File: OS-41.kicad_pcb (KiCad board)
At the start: 4 copper layers, 26.1 x 58.1 mm, 72 parts, among them J2 Conn_01x02_Pin, J3 Conn_01x02_Pin, J4 Conn_Coaxial, J6 Conn_01x04_Pin, J8 Conn_01x02_Pin, J9 Conn_01x02_Pin, U2 SI4432-B1-FMR, U3 MCP1640x-xCHY, U4 ATGM336H-5N31, U6 BMP390L, U7 STM32F411CEUx, Y1 Crystal_GND24, Y2 Crystal, Y3 Crystal_GND24

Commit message: Final PCB
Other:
- board text added: "BOOT"
- board text added: "RST"
- board text added: "Vin"
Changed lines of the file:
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@@
 		)
 		(property "Footprint" "centdir:ANT_1575AT_JOT"
-			(at 0 0 360)
+			(at 0 0 0)
 			(layer "F.Fab")
 			(hide yes)
@@
 		)
 		(property "Datasheet" ""
-			(at 0 0 360)
+			(at 0 0 0)
 			(layer "F.Fab")
 			(hide yes)
@@
 		)
 		(property "Description" "Antenna"
-			(at 0 0 360)
+			(at 0 0 0)
 			(layer "F.Fab")
 			(hide yes)
@@
 		(tags "capacitor handsolder")
 		(property "Reference" "C29"
-			(at 0.056569 1.06066 360)
+			(at 0.056569 1.06066 0)
 			(layer "F.SilkS")
 			(effects
@@
 		)
 		(property "Value" "1.5pF"
-			(at 0 1.16 360)
+			(at 0 1.16 0)
 			(layer "F.Fab")
 			(effects
@@
 		)
 		(fp_text user "${REFERENCE}"
-			(at 0 0 360)
+			(at 0 0 0)
 			(layer "F.Fab")
 			(effects
@@
 		(layer "Edge.Cuts")
 	)
+	(gr_text "GND"
+		(at 149.9 130.1 0)
+		(layer "B.SilkS")
+		(effects
+			(font
+				(size 1 1)
+				(thickness 0.25)
+				(bold yes)
+			)
+			(justify left bottom mirror)
+		)
+	)
+	(gr_text "Vin"
+		(at 146.3 130.1 0)
+		(layer "B.SilkS")
+		(effects
+			(font
+				(size 1 1)
+				(thickness 0.25)
+				(bold yes)
+			)
+			(justify left bottom mirror)
+		)
+	)
+	(gr_text "RST"
+		(at 128.62 109.9 -90)
+		(layer "B.SilkS")
+		(effects
+			(font
+				(size 1.5 1.5)
+				(thickness 0.3)
+				(bold yes)
+			)
+			(justify left bottom mirror)
+		)
+	)
+	(gr_text "GND"
+		(at 145.2 116.6 -90)
+		(layer "B.SilkS")
+		(effects
+			(font
+				(size 1 1)
+				(thickness 0.25)
+				(bold yes)
+			)
+			(justify left bottom mirror)
+		)
+	)
+	(gr_text "VCC"
+		(at 145.2 113.3 -90)
+		(layer "B.SilkS")
+		(effects
+			(font
+				(size 1 1)
+				(thickness 0.25)
+				(bold yes)
+			)
+			(justify left bottom mirror)
+		)
+	)
 	(gr_text "DIO"
 		(at 148.4 106.6 270)
@@
 		)
 	)
+	(gr_text "BOOT"
+		(at 128.79 100.52 270)
+		(layer "B.SilkS")
+		(effects
+			(font
+				(size 1.5 1.5)
+				(thickness 0.3)
+				(bold yes)
+			)
+			(justify left bottom mirror)
+		)
+	)
 	(gr_text "VCC"
 		(at 148.4 109.9 270)
@@
 			)
 		)
+	)
+	(zone
+		(net 0)
+		(net_name "")
+		(layers "F.Cu" "In1.Cu" "In2.Cu" "B.Cu")
+		(hatch edge 0.5)
+		(connect_pads
+			(clearance 0)
+		)
+		(min_thickness 0.25)
+		(filled_areas_thickness no)
+		(keepout
+			(tracks allowed)
+			(vias allowed)
+			(pads allowed)
+			(copperpour not_allowed)
+			(footprints allowed)
+		)
+		(fill
+			(thermal_gap 0.5)
+			(thermal_bridge_width 0.5)
+		)
+		(polygon
+			(pts
+				(xy 131.42 112.48) (xy 131.46 116.7) (xy 134.85 116.71) (xy 134.84 112.45) (xy 131.43 112.43)
+			)
+		)

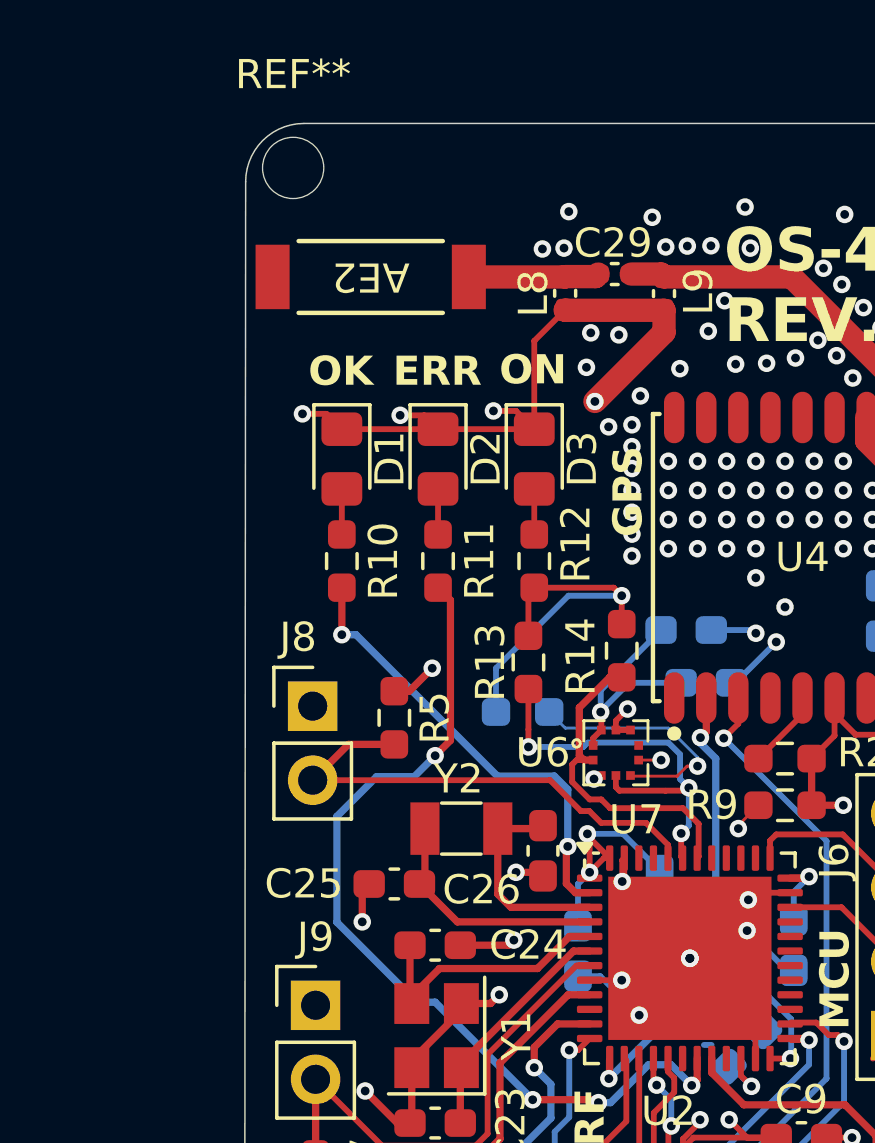
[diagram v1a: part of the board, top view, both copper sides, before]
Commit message: Add GPS text
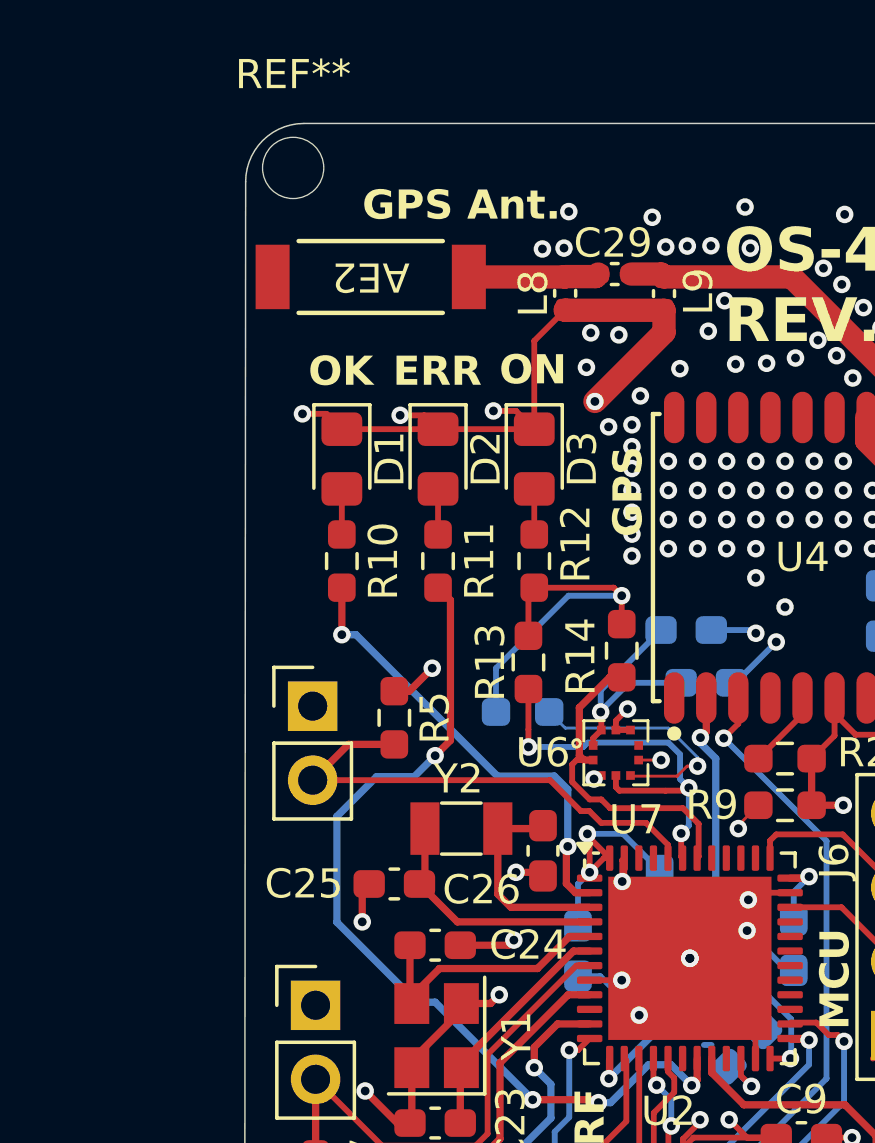
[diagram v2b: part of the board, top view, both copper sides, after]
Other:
- board text added: "GPS Ant."
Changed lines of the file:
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@@
 		(tags "Through hole pin header THT 1x02 2.54mm single row")
 		(property "Reference" "J9"
-			(at 0 -2.33 0)
-			(layer "F.SilkS")
+			(at 0 -2.33 -0)
+			(layer "B.SilkS")
 			(effects
 				(font
@@
 					(thickness 0.15)
 				)
+				(justify mirror)
 			)
 		)
@@
 		(tags "Through hole pin header THT 1x02 2.54mm single row")
 		(property "Reference" "J8"
-			(at -0.5 -2.36 0)
-			(layer "F.SilkS")
+			(at -0.5 -2.36 -0)
+			(layer "B.SilkS")
 			(effects
 				(font
@@
 					(thickness 0.15)
 				)
+				(justify mirror)
 			)
 		)
@@
 				(bold yes)
 			)
+			(justify left bottom)
+		)
+	)
+	(gr_text "GPS Ant."
+		(at 128.5 79.8 0)
+		(layer "F.SilkS")
+		(effects
+			(font
+				(size 1 1)
+				(thickness 0.25)
+				(bold yes)
+			)

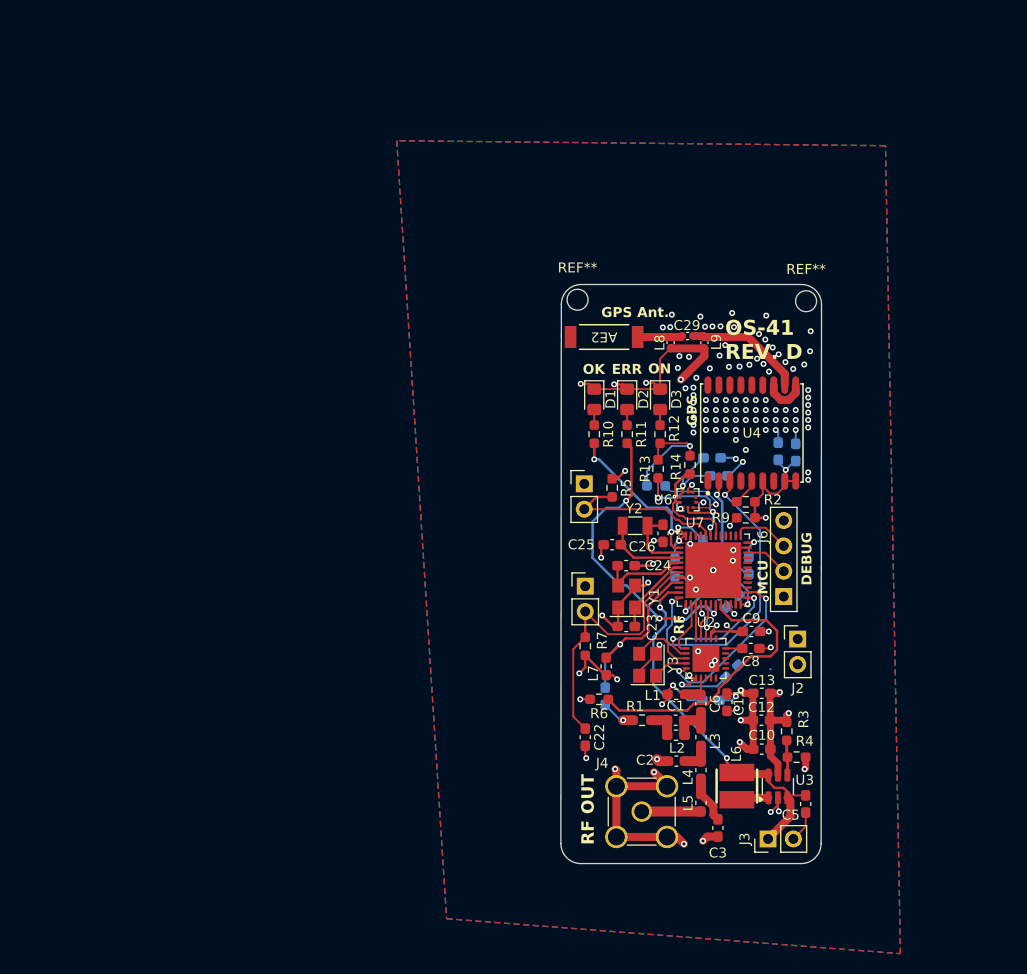
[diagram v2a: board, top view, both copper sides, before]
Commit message: Remaking the PCB... again...
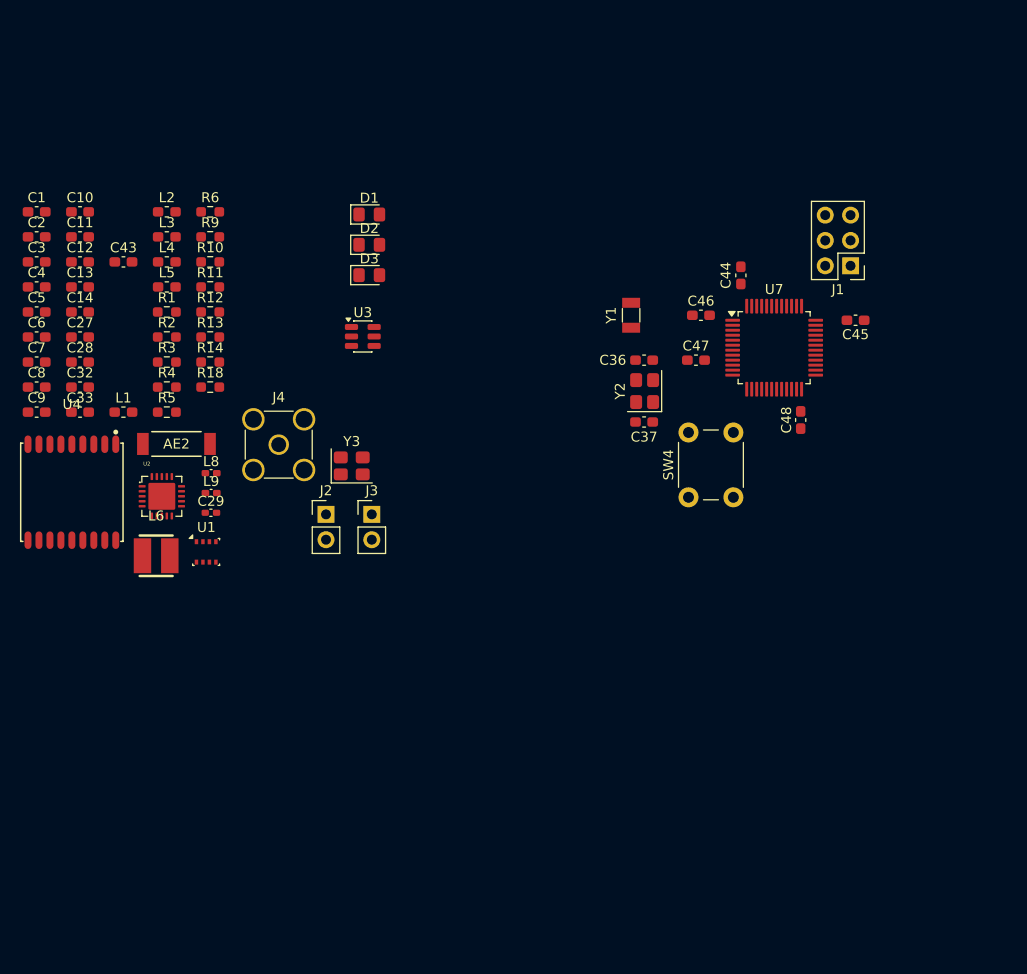
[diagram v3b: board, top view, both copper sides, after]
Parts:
- removed C15, C16, C17, C18, C19, C20, C22: 100nF, Capacitor_SMD:C_0603_1608Metric_Pad1.08x0.95mm_HandSolder
- removed C21: 2.2uF, Capacitor_SMD:C_0603_1608Metric_Pad1.08x0.95mm_HandSolder
- removed C23, C24, C25, C26: C, Capacitor_SMD:C_0603_1608Metric_Pad1.08x0.95mm_HandSolder
- removed J6: Conn_01x04_Pin, Connector_PinHeader_2.54mm:PinHeader_1x04_P2.54mm_Vertical
- removed J8, J9: Conn_01x02_Pin, Connector_PinHeader_2.54mm:PinHeader_1x02_P2.54mm_Vertical
- removed L7: 10uH, Inductor_SMD:L_0603_1608Metric_Pad1.05x0.95mm_HandSolder
- removed R7: 10k, Resistor_SMD:R_0603_1608Metric_Pad0.98x0.95mm_HandSolder
- removed REF** (x2): MountingHole_2.1mm, MountingHole:MountingHole_2.1mm
- removed U6: BMP390L, libsos41:LGA-10_L2.0-W2.0-P0.50-TL_BMP390L
- added C32: 15pF, Capacitor_SMD:C_0603_1608Metric_Pad1.08x0.95mm_HandSolder, F.Cu at (76.2, 86.7)
- added C33: 15pF, Capacitor_SMD:C_0603_1608Metric_Pad1.08x0.95mm_HandSolder, F.Cu at (76.2, 89.2)
- added C36: 14pF, Capacitor_SMD:C_0603_1608Metric_Pad1.08x0.95mm_HandSolder, F.Cu at (132.8, 84.0)
- added C37: 14pF, Capacitor_SMD:C_0603_1608Metric_Pad1.08x0.95mm_HandSolder, F.Cu at (132.8, 90.2)
- added C43: 10uF, Capacitor_SMD:C_0603_1608Metric_Pad1.08x0.95mm_HandSolder, F.Cu at (80.6, 74.2)
- added C44: 100nF, Capacitor_SMD:C_0603_1608Metric_Pad1.08x0.95mm_HandSolder, F.Cu at (142.5, 75.5)
- added C45: 100nF, Capacitor_SMD:C_0603_1608Metric_Pad1.08x0.95mm_HandSolder, F.Cu at (154.0, 80.0)
- added C46: 100nF, Capacitor_SMD:C_0603_1608Metric_Pad1.08x0.95mm_HandSolder, F.Cu at (138.5, 79.5)
- added C47: 100nF, Capacitor_SMD:C_0603_1608Metric_Pad1.08x0.95mm_HandSolder, F.Cu at (138.0, 84.0)
- added C48: 100nF, Capacitor_SMD:C_0603_1608Metric_Pad1.08x0.95mm_HandSolder, F.Cu at (148.5, 90.0)
- added J1: Conn_02x03_Counter_Clockwise, Connector_PinHeader_2.54mm:PinHeader_2x03_P2.54mm_Vertical, F.Cu at (153.5, 74.5)
- added SW4: SW_Push, Button_Switch_THT:SW_PUSH_6mm, F.Cu at (137.2, 97.8)
- added U1: BME280, Package_LGA:Bosch_LGA-8_2.5x2.5mm_P0.65mm_ClockwisePinNumbering, F.Cu at (88.9, 103.2)
- C14, C27, C28, C7, R18: moved to F.Cu
- C4: value 10uF -> 100nF; moved to F.Cu
- U7: value STM32F411CEUx -> STM32F103C8Tx; footprint Package_DFN_QFN:QFN-48-1EP_7x7mm_P0.5mm_EP5.6x5.6mm -> Package_QFP:LQFP-48_7x7mm_P0.5mm
- Y1: value Crystal_GND24 -> 32.768KHz 12.5pF; footprint Crystal:Crystal_SMD_3225-4Pin_3.2x2.5mm -> Crystal:Crystal_SMD_3215-2Pin_3.2x1.5mm
- Y2: value Crystal -> 8MHz 12pF; footprint Crystal:Crystal_SMD_3215-2Pin_3.2x1.5mm -> Crystal:Crystal_SMD_3225-4Pin_3.2x2.5mm
- Y3: value Crystal_GND24 -> 30MHz 10pF
- moved C5 91.5 mm to (71.9, 79.2), turned to 0 degrees
- moved C3 88.8 mm to (71.9, 74.2), turned to 0 degrees
- moved C10 87.0 mm to (76.2, 69.1), turned to 0 degrees
- moved C2 82.9 mm to (71.9, 71.6)
- moved C12 82.3 mm to (76.2, 74.2), turned to 0 degrees
- moved C1 81.9 mm to (71.9, 69.1)
- moved C11 79.9 mm to (76.2, 71.6), turned to 0 degrees
- moved C13 79.6 mm to (76.2, 76.7), turned to 0 degrees
- moved C4 79.3 mm to (71.9, 76.7)
- moved C7 76.3 mm to (71.9, 84.2), turned to 0 degrees
- moved C8 76.2 mm to (71.9, 86.7)
- moved C6 76.1 mm to (71.9, 81.7), turned to 0 degrees
- moved C9 75.0 mm to (71.9, 89.2)
- moved L5 74.4 mm to (85.0, 76.7), turned to 0 degrees
- moved L4 73.9 mm to (85.0, 74.2), turned to 0 degrees
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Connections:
- R5 pad 1: BOOT0 -> VCC_3.3
- R5 pad 2: GND -> RST
- R6 pad 1: PB2 -> Net-(U7-BOOT0)
- U7 pad 14: NSEL -> unconnected-(U7-PA4-Pad14)
- U7 pad 15: SCLK -> unconnected-(U7-PA5-Pad15)
- U7 pad 16: SDO -> unconnected-(U7-PA6-Pad16)
- U7 pad 17: SDI -> unconnected-(U7-PA7-Pad17)
- U7 pad 19: LED_ERR -> unconnected-(U7-PB1-Pad19)
- U7 pad 2: LED_OK -> unconnected-(U7-PC13-Pad2)
- U7 pad 20: PB2 -> unconnected-(U7-PB2-Pad20)
- U7 pad 22: Net-(U7-VCAP1) -> unconnected-(U7-PB11-Pad22)
- U7 pad 25: NIRQ -> unconnected-(U7-PB12-Pad25)
- U7 pad 26: SDN -> unconnected-(U7-PB13-Pad26)
- U7 pad 27: GPIO4 -> unconnected-(U7-PB14-Pad27)
- U7 pad 28: GPIO5 -> unconnected-(U7-PB15-Pad28)
- U7 pad 29: GPIO7 -> unconnected-(U7-PA8-Pad29)
- U7 pad 3: OSC32_IN -> RCC_OSC32_IN
- U7 pad 30: GPIO0 -> unconnected-(U7-PA9-Pad30)
- U7 pad 31: GPIO1 -> unconnected-(U7-PA10-Pad31)
- U7 pad 34: SWDIO -> SYS_JTMS-SWDIO
- U7 pad 37: SWCLK -> SYS_JTCK-SWCLK
- U7 pad 39: DQ -> unconnected-(U7-PB3-Pad39)
- U7 pad 4: OSC32_OUT -> RCC_OSC32_OUT
- U7 pad 44: BOOT0 -> Net-(U7-BOOT0)
- U7 pad 45: GPIO6 -> unconnected-(U7-PB8-Pad45)
- U7 pad 5: OSC_IN -> X_IN
- U7 pad 6: OSC_OUT -> X_OUT
- U7 pad 7: NRST -> RST
- U7 pad 9: VREF -> VCC
- Y1 pad 1: OSC_OUT -> RCC_OSC32_IN
- Y1 pad 2: GND -> RCC_OSC32_OUT
- Y2 pad 1: OSC32_OUT -> X_OUT
- Y2 pad 2: OSC32_IN -> GND
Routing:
- net GND: track 155.5 -> 0.00 mm, vias 127 -> 0
- net VCC: track 113.2 -> 0.00 mm, vias 19 -> 0
- net BATT: track 38.1 -> 0.00 mm, vias 2 -> 0
- net RXD: track 30.8 -> 0.00 mm, vias 2 -> 0
- net LED_ERR: track 30.6 -> 0.00 mm, vias 4 -> 0
- net PB2: track 29.1 -> 0.00 mm
- net NRST: track 27.2 -> 0.00 mm
- net SDN: track 17.0 -> 0.00 mm, vias 2 -> 0
- net VREF: track 16.9 -> 0.00 mm, vias 1 -> 0
- net BOOT0: track 16.9 -> 0.00 mm
- net LED_OK: track 15.9 -> 0.00 mm, vias 2 -> 0
- net TXD: track 15.6 -> 0.00 mm, vias 2 -> 0
- net SDA: track 14.2 -> 0.00 mm, vias 3 -> 0
- net NIRQ: track 13.3 -> 0.00 mm, vias 2 -> 0
- net Net-(U4-RF_IN): track 11.9 -> 0.00 mm
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- removed copper zone on B.Cu, net GND
- removed copper zone on F.Cu, net GND
- removed copper zone on In1.Cu, net GND
- removed copper zone on In2.Cu, net VCC
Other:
- board outline removed
- board text removed: "BOOT"
- board text removed: "CLK"
- board text removed: "DEBUG"
- board text removed: "DIO"
- board text removed: "ERR"
- board text removed: "GND"
- board text removed: "GPS"
- board text removed: "GPS Ant."
- board text removed: "MCU"
- board text removed: "OK"
- board text removed: "ON"
- board text removed: "OS-41 REV. D"
- board text removed: "RF"
- board text removed: "RF OUT"
- board text removed: "RST"
- board text removed: "To infinity and beyond!"
- board text removed: "VCC"
- board text removed: "Vin"

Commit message: Continue layout
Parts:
- SW4: footprint Button_Switch_THT:SW_PUSH_6mm -> libsos41:SMD_SW_NEW_REDONE
- moved U4 75.4 mm to (143.8, 65.4), turned to 180 degrees
- moved L9 72.1 mm to (147.0, 54.0), turned to -90 degrees
- moved C29 71.4 mm to (145.0, 54.6), turned to 180 degrees
- moved L8 67.7 mm to (143.0, 54.0), turned to -90 degrees
- moved AE2 63.2 mm to (133.8, 51.2), turned to 180 degrees
- moved U2 61.1 mm to (145.5, 95.2), turned to 90 degrees
- moved C32 56.4 mm to (131.7, 76.0)
- moved C33 55.9 mm to (131.7, 82.0)
- moved C14 55.5 mm to (131.4, 73.4)
- moved U1 55.2 mm to (135.6, 73.8), turned to -90 degrees
- moved Y3 34.3 mm to (137.8, 95.6), turned to 90 degrees
- moved SW4 20.9 mm to (154.0, 85.3)
- moved Y1 1.32 mm to (132.7, 79.0)
- moved J1 0.99 mm to (154.0, 75.4)
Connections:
- U7 pad 14: unconnected-(U7-PA4-Pad14) -> NSEL
- U7 pad 15: unconnected-(U7-PA5-Pad15) -> SCLK
- U7 pad 16: unconnected-(U7-PA6-Pad16) -> SDO
- U7 pad 17: unconnected-(U7-PA7-Pad17) -> SDI
- U7 pad 29: unconnected-(U7-PA8-Pad29) -> NIRQ
- U7 pad 30: unconnected-(U7-PA9-Pad30) -> SDN
